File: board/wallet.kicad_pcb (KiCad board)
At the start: 4 copper layers, 48 x 85 mm, 111 parts, among them J1 TYPE-C-31-M-12, U1 BQ25185DLHR, U11 E73-2G4M08S1C, U12 ME6211C28M5G-N, U13 TPS60230RGTR, U14 TLV70313DBVR, U15 MAX17048G+T10, U16 SLS32AIA010MK, U2 TPS63802DLAR, U4 STM32U585VIT6Q, U5 SE050E2HQ1/Z01Z3Z, U6 TS3USB221ARSER, U7 SN74LVC1G02DBVR(UMW), U8 TPS22917DBVR, U9 TXU0202DCUR

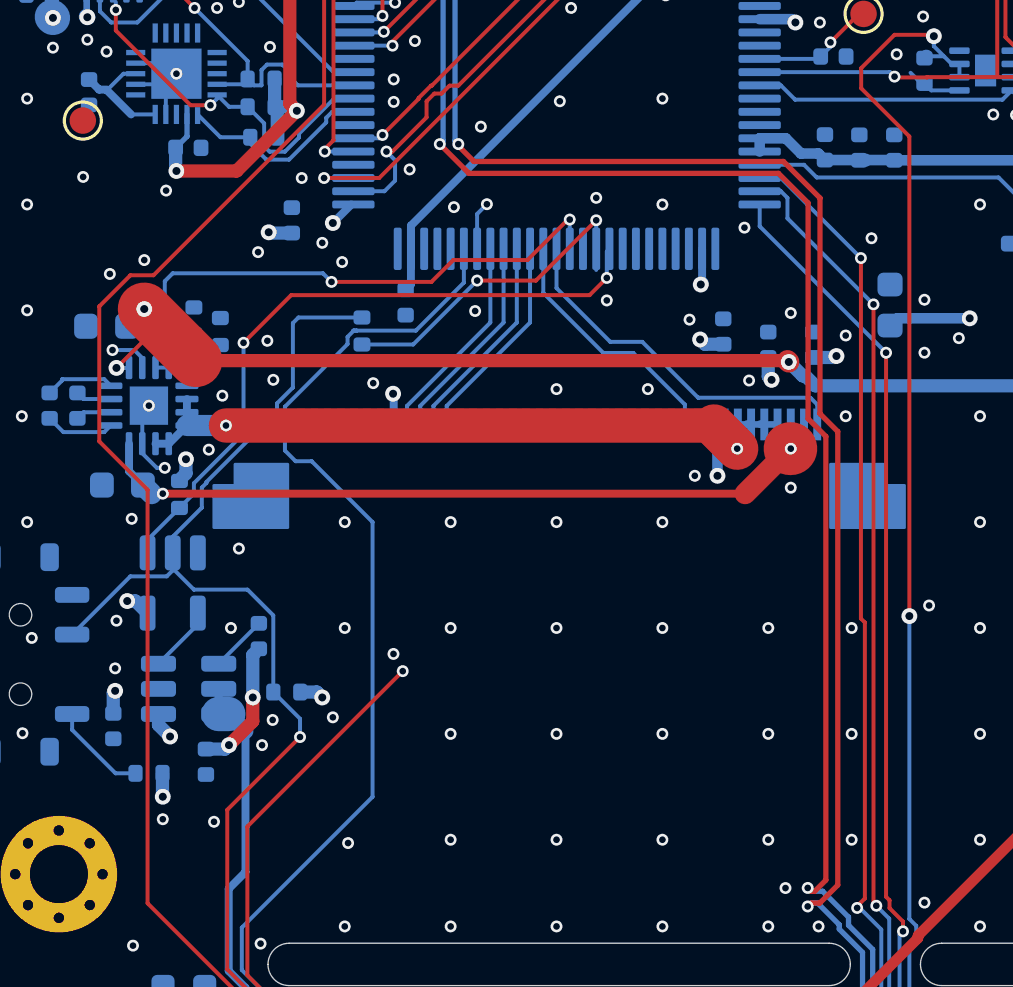
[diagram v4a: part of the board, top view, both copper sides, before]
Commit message: Owner: RADIO_TXD routed; USB pair, backlight and 3.3 V touch-ups
RADIO_TXD 67.6 mm (62.8 front, 4.8 back, 2 vias), around the J_TFT row since
RADIO_RXD holds the only slot through it. USB_MCU pair, BL_A/BL_K, SYS, V3V3
and AIRGAP_SENSE nudged.

As committed: three GND stitching vias at (18.0,50.0), (22.0,46.0), (26.0,46.0)
were shoved 0.3-0.5 mm by KiCad's interactive router and came back on V3V3,
connected to nothing (the "3.3 V vias" the owner saw); a 0.16 mm TXD crumb;
J_TFT pin 10 cut off from the pour by the backlight reroute. Fixed next.

Co-Authored-By: Claude Opus 5.5 <noreply@anthropic.com>
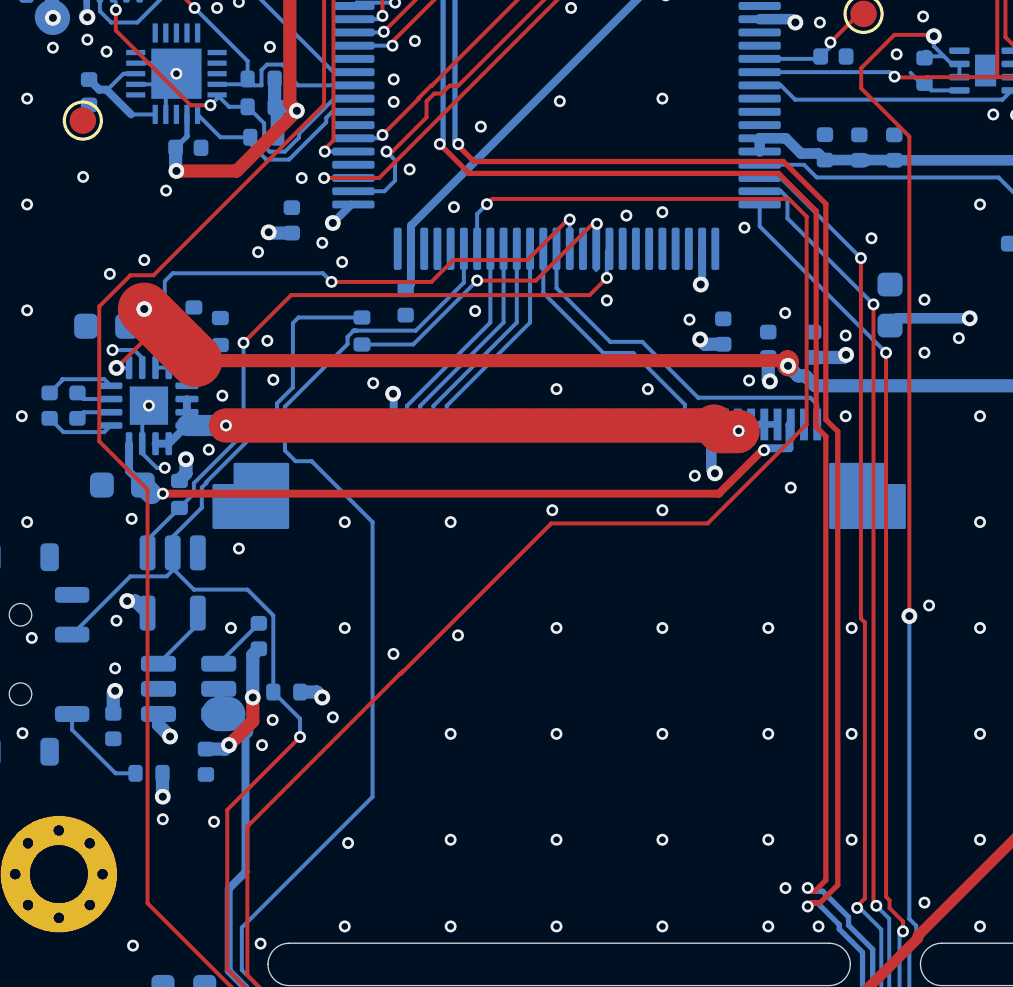
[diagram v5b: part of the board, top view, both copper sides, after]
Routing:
- net RADIO_TXD_MCU: track 28.0 -> 67.6 mm, vias 3 -> 2
- net V3V3: track 135.3 -> 135.6 mm, vias 45 -> 48
- net GND: vias 264 -> 261

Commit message: Fully routed, DRC clean: re-netted stitching vias restored and made free
DRC: 0 violations, 0 unconnected.
- The three GND stitching vias KiCad's interactive router shoved onto the 3.3 V
  plane are GND again, and all 229 track-less GND vias are now "free" vias,
  so a shove during hand routing keeps their net.
- J_TFT pin 10 (0.3 mm at 0.5 mm pitch) is boxed in by the backlight reroute,
  so the pour cannot reach it; a straight 0.2 mm track runs 0.7 mm past its
  end into the pour (solid connection was already set and is not enough).
- RADIO_TXD 0.16 mm crumb removed.
Gates pass; cleanCopper --check clean; no GND pad-to-via ties beyond the 9 kept.

Co-Authored-By: Claude Opus 5.5 <noreply@anthropic.com>
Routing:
- net GND: track 38.3 -> 39.5 mm, vias 261 -> 264
- net V3V3: vias 48 -> 45

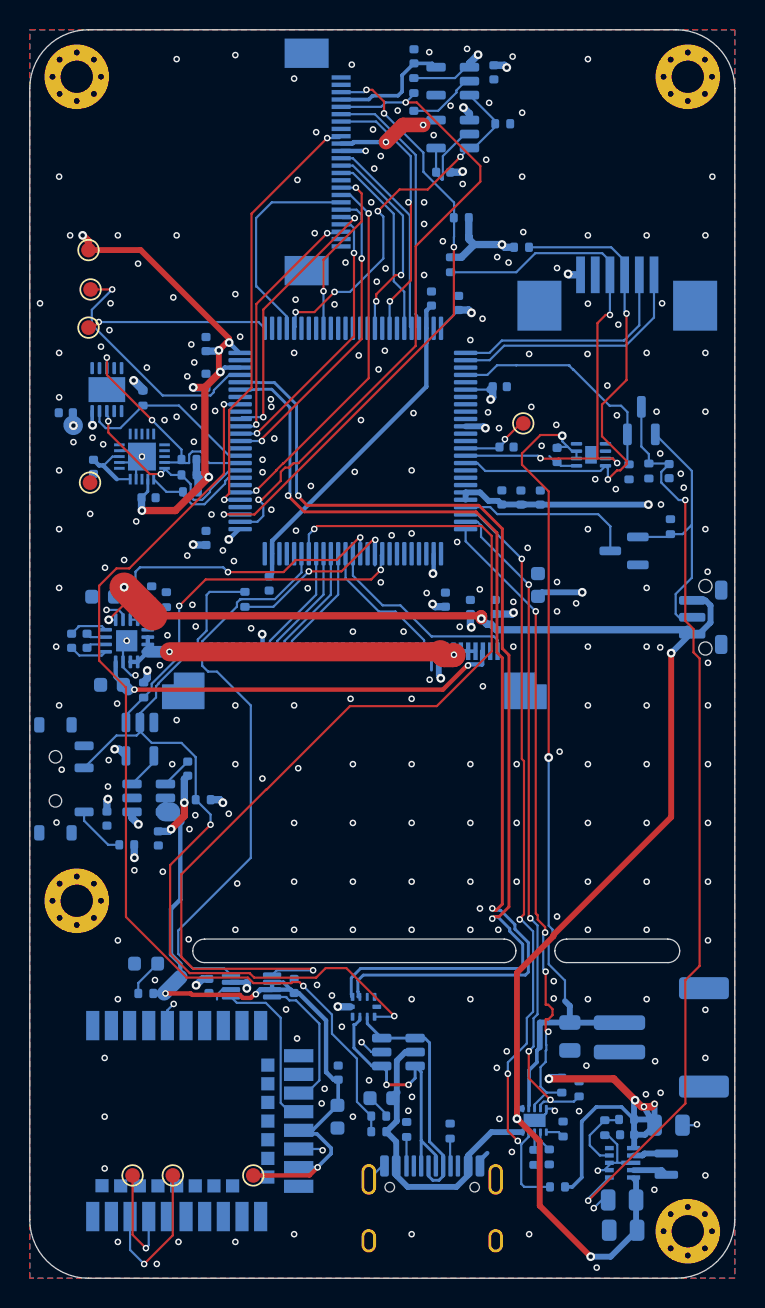
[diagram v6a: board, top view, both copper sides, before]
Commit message: Router tidy pass: 98 stacked/split segments gone, copper unchanged
humanRouter --tidy=only (working tree on 2f214cb, the peer's tidy not yet
committed; checked here): 97 segments lying on an equal-or-wider segment of
their net removed, 1 collinear split merged; every removal KiCad's DRC objected
to rolled back (the load-bearing stubs on J_TFT pin 10, C_GAUGE, U9 pin 2 and
eight "dangling" ends that are T-junctions). 1032 -> 934 tracks; per net and
layer the copper differs by at most 0.001 mm^2 (end rounding). DRC: 0
violations, 0 unconnected.

cleanCopper counts copper overlapping a pad as joined to it, as KiCad does, not
only a track end inside the pad: after tidy, three pieces reach their pad by
overlap and were misread as stale.

Co-Authored-By: Claude Opus 5.5 <noreply@anthropic.com>
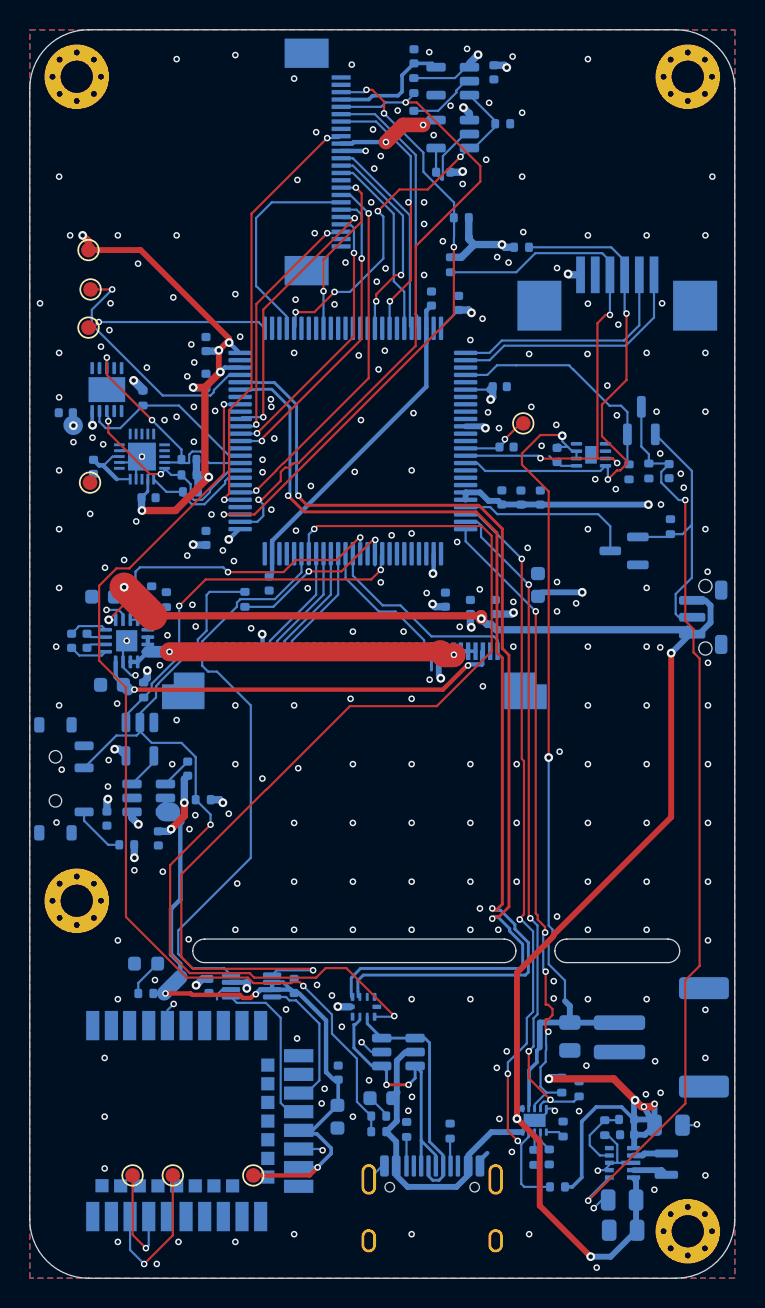
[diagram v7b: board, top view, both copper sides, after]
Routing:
- net GND: track 39.5 -> 36.1 mm
- net USB_DN: track 16.6 -> 13.9 mm
- net VBUS: track 21.5 -> 18.9 mm
- net V3V3: track 135.6 -> 133.1 mm
- net RADIO_3V3: track 48.7 -> 46.9 mm
- net USB_DP: track 18.3 -> 16.6 mm
- net AIRGAP: track 57.1 -> 55.8 mm
- net CHG_CE: track 46.0 -> 44.9 mm
- net SYS: track 105.2 -> 104.2 mm
- net BTN: track 18.7 -> 17.8 mm
- net CHG_STAT1: track 52.4 -> 51.5 mm
- net SE_SCL: track 13.8 -> 12.9 mm
- net CAM_D4: track 14.6 -> 13.8 mm
- net SE_ENA: track 7.34 -> 6.54 mm
- net I2C_SDA: track 33.8 -> 33.0 mm
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
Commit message: Owner: redundant 3.3 V copper removed, reroutes tightened, C_VUSB closer
27 V3V3 tracks (52.7 mm) that duplicated the In1 plane removed (V3V3 track
133 -> 92 mm), GND tracks 36 -> 28 mm; small reroutes on SE_SDA, I2C_SDA/SCL,
CHG_*, CAM_*, AIRGAP, PWR_HOLD, CTP_INT; C_VUSB 0.6 mm closer to VDDUSB.

As committed: USB-C GND pin A1 cut off from its shell (1 unconnected), a 0.2 mm
PWR_HOLD stub, U12's GND pad thermally starved -- fixed next.

Co-Authored-By: Claude Opus 5.5 <noreply@anthropic.com>
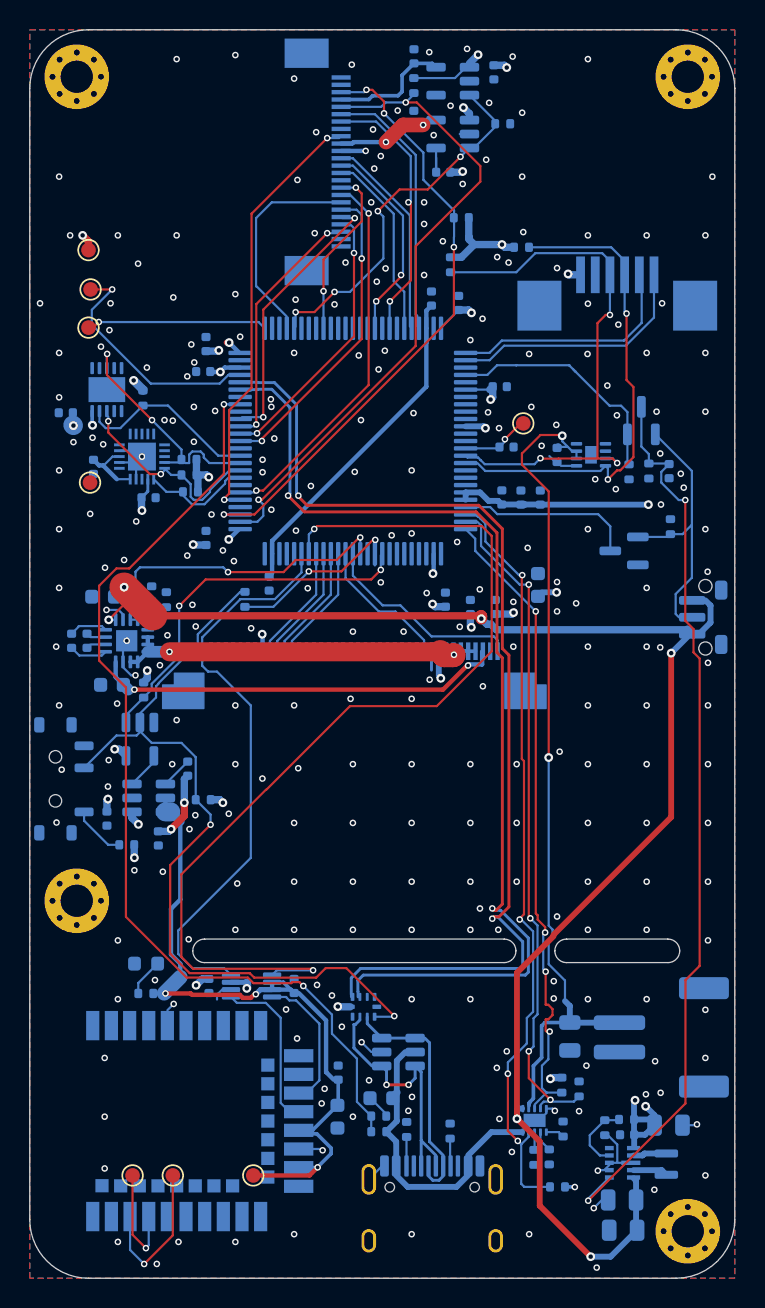
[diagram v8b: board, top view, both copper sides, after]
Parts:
- moved C_VUSB 0.66 mm to (11.8, 23.3), turned to 180 degrees
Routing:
- net V3V3: track 133.1 -> 84.4 mm, vias 45 -> 44
- net GND: track 36.1 -> 27.8 mm
- net AIRGAP: track 55.8 -> 54.6 mm
- net I2C_SDA: track 33.0 -> 32.0 mm
- net SE_SDA: track 15.6 -> 16.1 mm
